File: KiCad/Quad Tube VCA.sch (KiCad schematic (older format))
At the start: 236 parts, among them IC1 TL072, IC10 LM358, IC11 TL072, IC12 TL072, IC2 TL072, IC3 LM358, IC4 TL072, IC5 LM358, IC6 TL072, IC7 TL072, IC8 LM358, IC9 TL072

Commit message: 1.3 pcb update
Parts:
- removed C55, C56, C57, C58: 100nf, Capacitor_SMD:C_0603_1608Metric, symbol Device:C_Small
- removed IC11, IC12: TL072, Package_SO:SOIC-8_3.9x4.9mm_P1.27mm, symbol Amplifier_Operational:TL072
- removed R100, R101: 100k, Resistor_SMD:R_0603_1608Metric, symbol Device:R_Small_US
- R13, R37, R61, R85: footprint Resistor_SMD:R_1206_3216Metric -> Resistor_SMD:R_1210_3225Metric
- R2, R25, R49, R73: value 100k -> 33k
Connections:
- net GND: now also R96.2, R97.2, R98.2, R99.2; no longer IC2.3 (+), IC2.5 (+), IC7.3 (+), IC7.5 (+)
- net at J_OUT1.2: now also R30.2; no longer R97.2
- net at IC2.2 (-), R7.2: now also R96.1; no longer R9.1
- net at R30.1, R34.1: now also IC2.5 (+); no longer IC2.6 (-), R31.2
- net at J_OUT2.2: now also R54.2; no longer R99.2
- net at IC7.2 (-), R55.2: now also R98.1; no longer R54.1, R58.1
- net at R79.1, R81.1: now also IC7.5 (+); no longer IC7.6 (-), R78.2
- net at R97.1: now also IC2.6 (-), R31.2; no longer R96.2
- net at J_OUT3.2: now also R79.2
- net at R99.1: now also IC7.6 (-), R78.2; no longer R98.2
- new net: IC2.3 (+), R9.1
- new net: IC7.3 (+), R54.1, R58.1

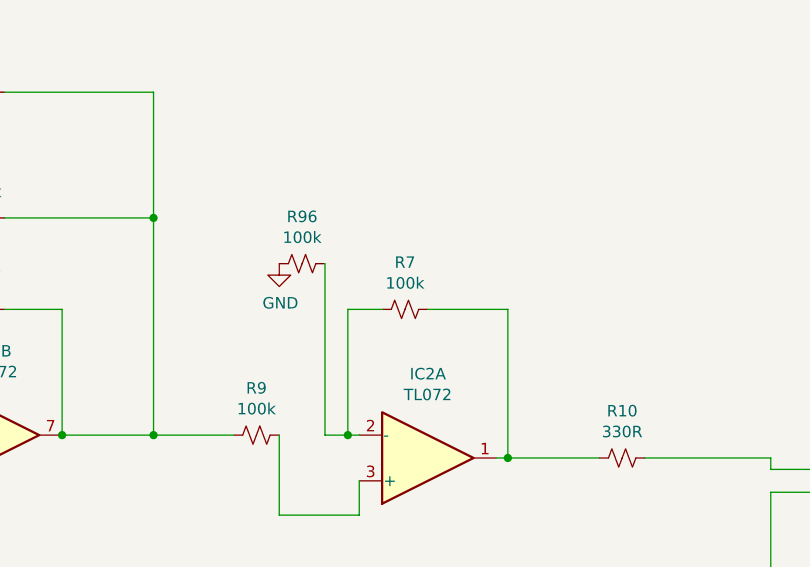
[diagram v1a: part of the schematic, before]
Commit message: updates feedback resistor value for vca1
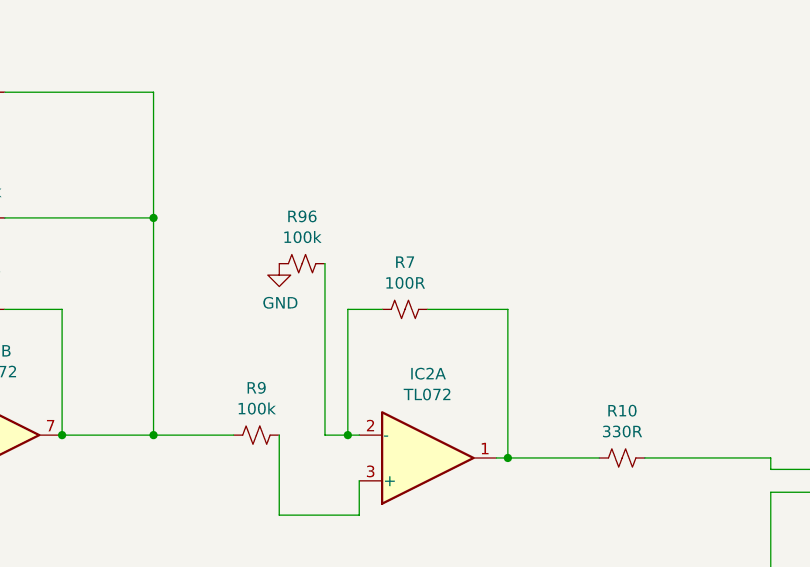
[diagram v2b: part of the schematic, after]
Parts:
- R7: value 100k -> 100R
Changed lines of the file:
@@
 P 11150 3300
 F 0 "R7" V 10945 3300 50  0000 C CNN
-F 1 "100k" V 11036 3300 50  0000 C CNN
+F 1 "100R" V 11036 3300 50  0000 C CNN
 F 2 "Resistor_SMD:R_0603_1608Metric" H 11150 3300 50  0001 C CNN
 F 3 "~" H 11150 3300 50  0001 C CNN

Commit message: v1.3 release
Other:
- note added: "“Vālvs”!!"
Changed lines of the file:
@@
 Wire Wire Line
 	11150 21400 11200 21400
+Text Notes 12950 27300 0    50   ~ 0
+“Vālvs”!!
 $EndSCHEMATC
